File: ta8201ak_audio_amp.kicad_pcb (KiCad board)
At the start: 2 copper layers, 40.3 x 38 mm, 16 parts, among them J1 INPUT, J2 OUTPUT, J3 POWER, U1 TA8201AK

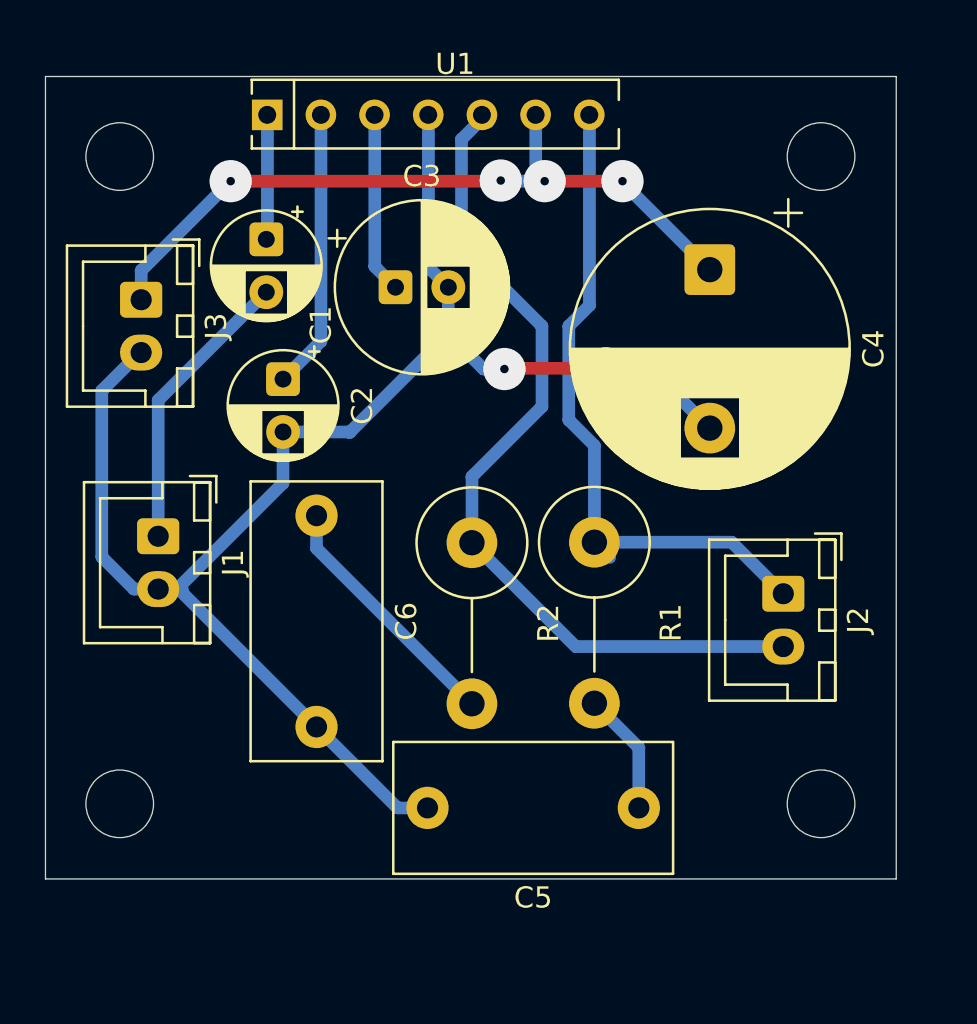
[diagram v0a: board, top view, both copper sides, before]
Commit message: 抵抗560Ωを追加Cを3.3uF,33uFに変更
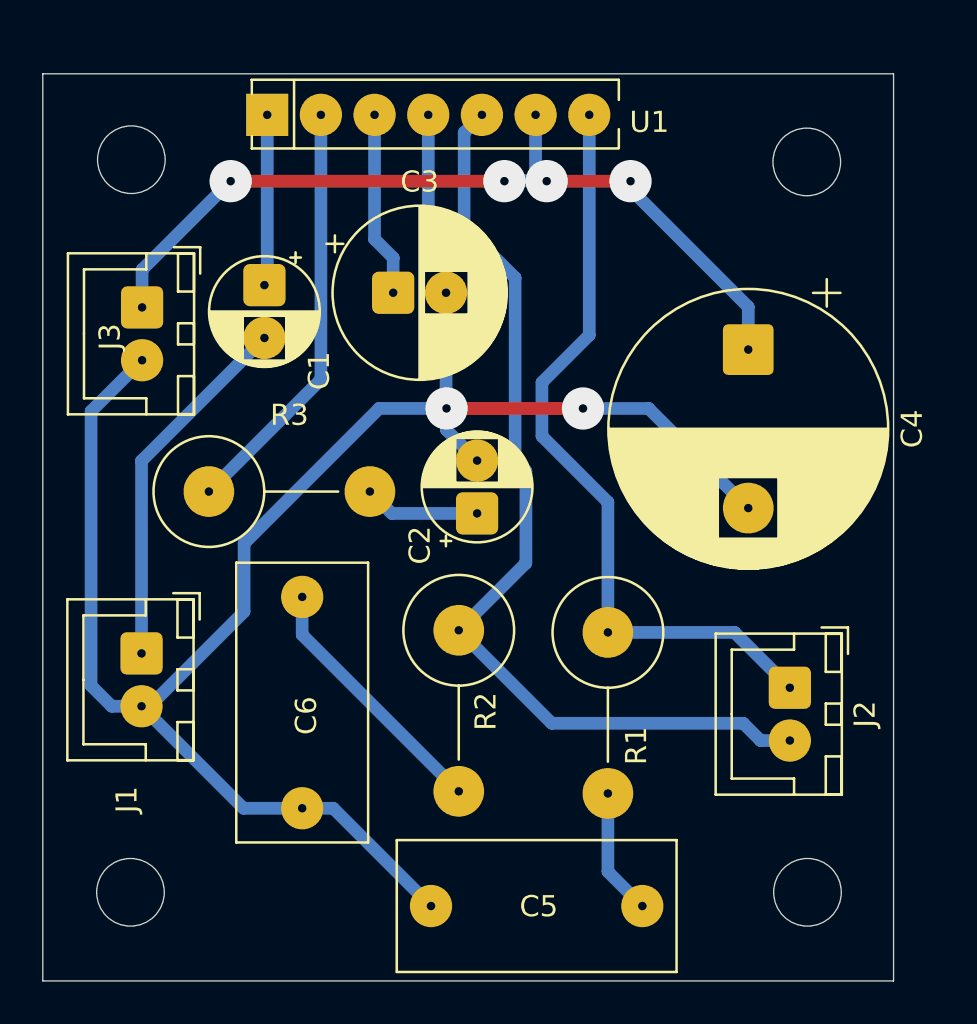
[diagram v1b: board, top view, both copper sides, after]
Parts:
- added R3: 560, Resistor_THT:R_Axial_DIN0516_L15.5mm_D5.0mm_P7.62mm_Vertical, F.Cu at (118.6, 66.8)
- C1: value 4.7uF -> 3.3uF
- C2: value 47uF -> 33uF
- moved C2 11.2 mm to (131.3, 67.8), turned to 90 degrees
- moved J1 5.60 mm to (115.4, 74.4)
- moved C5 4.65 mm to (139.1, 86.4)
- moved J2 4.46 mm to (146.1, 76.0)
- moved R1 4.32 mm to (137.5, 73.4)
- moved H4 4.24 mm to (146.9, 85.7)
- moved H3 4.22 mm to (114.9, 85.7)
- moved C4 4.20 mm to (144.1, 60.0)
- moved R2 4.19 mm to (130.4, 73.3)
- moved C6 3.91 mm to (123.0, 71.7)
- moved C1 2.17 mm to (121.2, 57.0)
- moved H2 0.72 mm to (146.9, 51.2)
- moved H1 0.57 mm to (114.9, 51.1)
- moved J3 0.37 mm to (115.4, 58.0)
- moved C3 0.28 mm to (127.3, 57.4)
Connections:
- C2 pad 1: Net-(U1-NF) -> Net-(C2-Pad1)
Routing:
- net GND: track 78.3 -> 93.3 mm
- net Net-(U1-NF): track 13.1 -> 20.0 mm
- net VCC: track 36.1 -> 41.7 mm
- net Net-(C2-Pad1): track 0.00 -> 5.50 mm
- net Net-(J2-Pin_2): track 40.5 -> 45.5 mm
- net Net-(J2-Pin_1): track 31.9 -> 36.4 mm
- net Net-(C1-Pad2): track 13.7 -> 17.3 mm
- net Net-(U1-IN): track 5.73 -> 8.11 mm
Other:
- board size 40.3 x 38 mm -> 40.3 x 42.9 mm

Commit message: 配置の修正
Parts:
- moved C4 1.64 mm to (144.1, 61.7), turned to 180 degrees
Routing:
- net GND: track 93.3 -> 84.3 mm, vias 2 -> 1
- net Net-(J2-Pin_2): track 45.5 -> 51.7 mm
- net VCC: track 41.7 -> 43.2 mm
- net Net-(J2-Pin_1): track 36.4 -> 37.8 mm

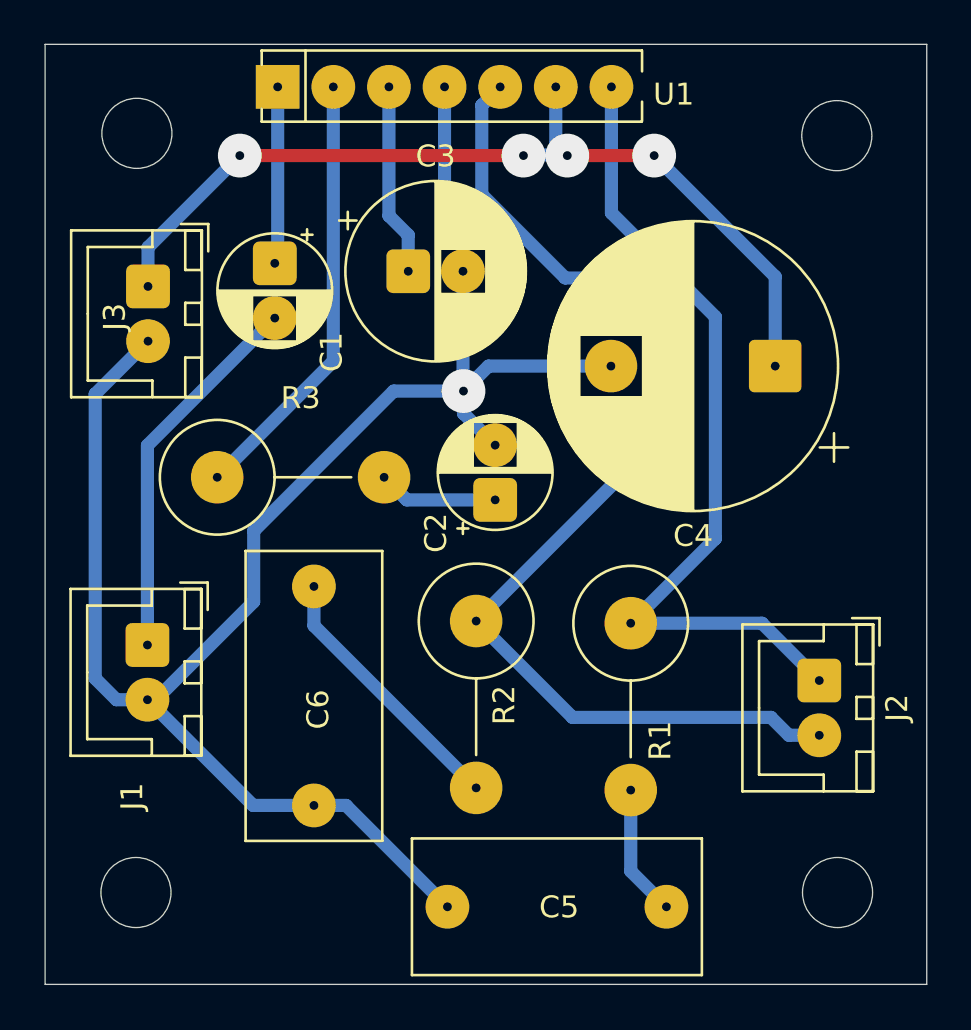
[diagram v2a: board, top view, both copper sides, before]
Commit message: 配置変更、ジャンパを減らす。
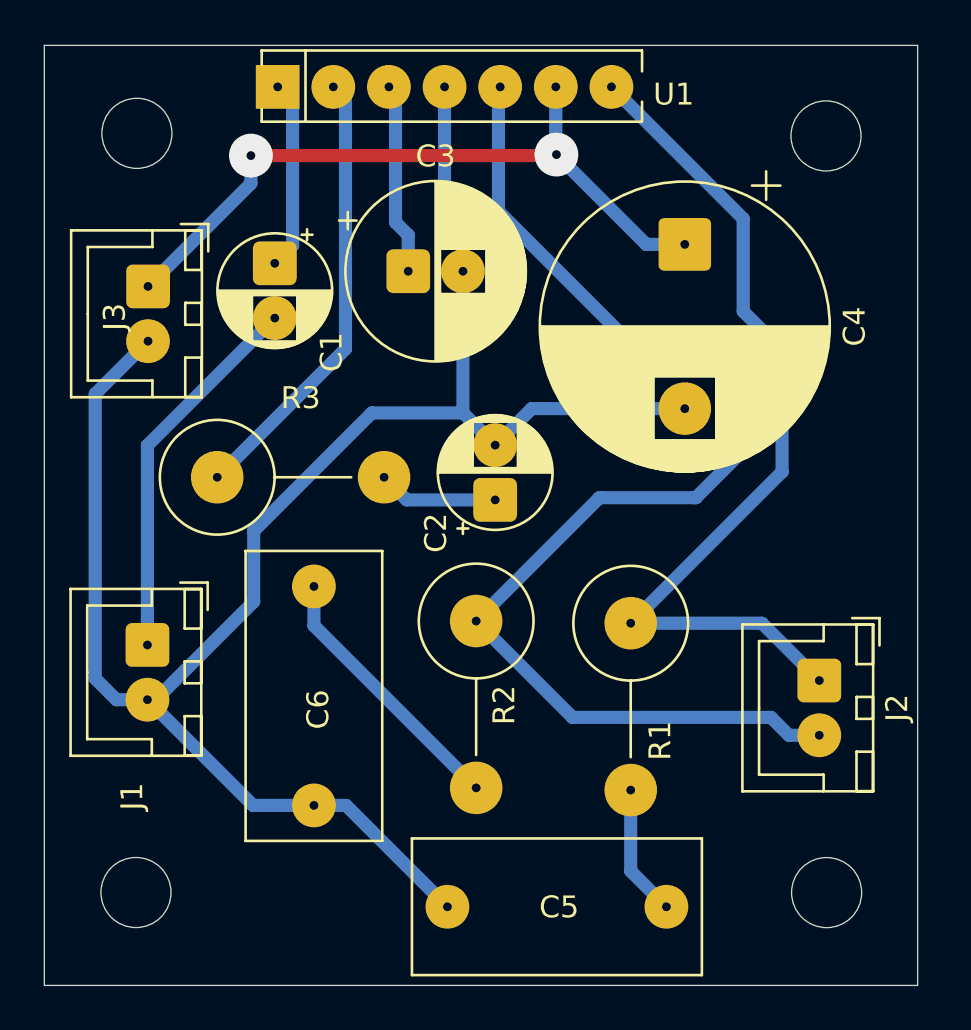
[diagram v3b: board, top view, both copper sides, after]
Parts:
- moved C4 6.92 mm to (140.0, 56.1), turned to -90 degrees
- moved H4 0.50 mm to (146.4, 85.7)
- moved H2 0.49 mm to (146.4, 51.2)
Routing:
- net VCC: track 43.2 -> 34.5 mm, vias 4 -> 2
- net Net-(J2-Pin_2): track 51.7 -> 57.3 mm
- net Net-(J2-Pin_1): track 37.8 -> 40.3 mm
- net GND: track 84.3 -> 85.7 mm, vias 1 -> 0
- net Net-(U1-IN): track 8.11 -> 8.68 mm
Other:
- board size 40.3 x 42.9 mm -> 39.9 x 42.9 mm

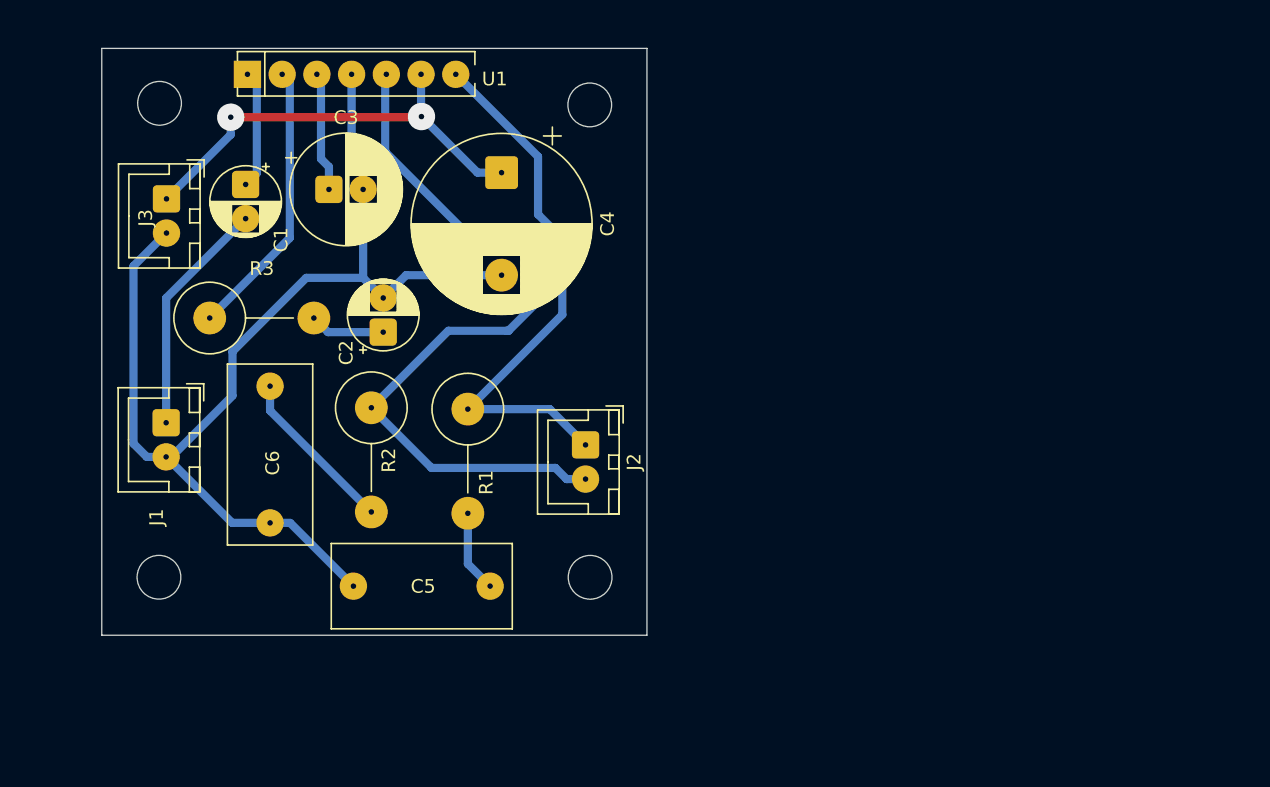
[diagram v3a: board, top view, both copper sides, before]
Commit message: 配置変更、アッテネーター追加、ベタ追加。
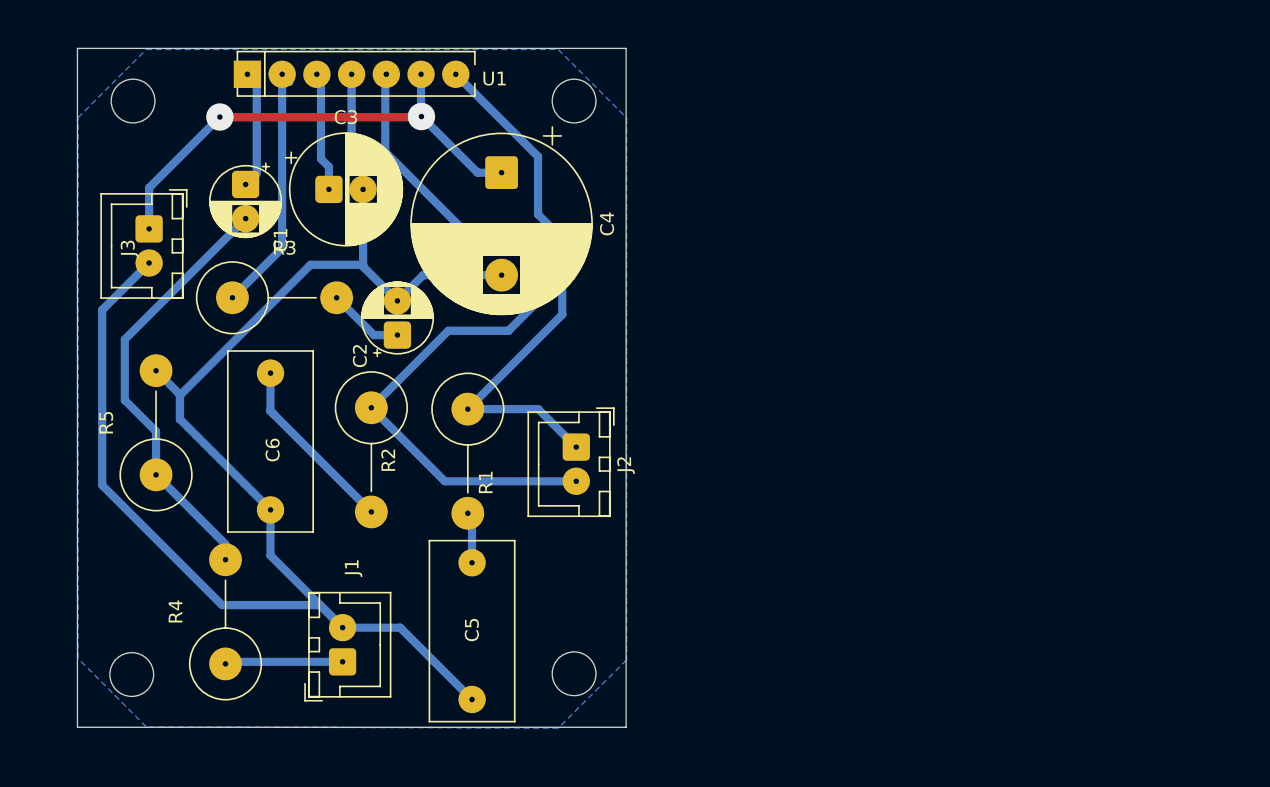
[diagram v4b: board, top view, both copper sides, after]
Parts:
- added R4: 39kΩ, Resistor_THT:R_Axial_DIN0516_L15.5mm_D5.0mm_P7.62mm_Vertical, F.Cu at (119.8, 92.1)
- added R5: 10kΩ, Resistor_THT:R_Axial_DIN0516_L15.5mm_D5.0mm_P7.62mm_Vertical, F.Cu at (114.7, 78.2)
- moved J1 21.7 mm to (128.3, 91.9), turned to 90 degrees
- moved H3 7.39 mm to (112.9, 92.8)
- moved H4 7.15 mm to (145.3, 92.8)
- moved J3 2.54 mm to (114.2, 60.2)
- moved R3 2.23 mm to (120.3, 65.3)
- moved C5 2.16 mm to (137.8, 84.7), turned to -90 degrees
- moved H1 1.94 mm to (113.0, 50.9)
- moved H2 1.18 mm to (145.3, 50.9)
- moved C2 1.06 mm to (132.3, 68.0)
- moved C6 0.95 mm to (123.1, 70.8)
- moved J2 0.70 mm to (145.4, 76.2)
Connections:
- J1 pad T: Net-(C1-Pad2) -> Net-(J1-PadT)
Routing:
- net GND: track 85.7 -> 122.1 mm
- net Net-(C1-Pad2): track 17.3 -> 31.7 mm
- net Net-(J1-PadT): track 0.00 -> 8.63 mm
- net VCC: track 34.5 -> 36.9 mm
- net Net-(C5-Pad1): track 6.00 -> 3.75 mm
- net Net-(U1-NF): track 20.5 -> 18.6 mm
- net Net-(C6-Pad1): track 12.3 -> 13.6 mm
- net Net-(J2-Pin_2): track 57.3 -> 56.7 mm
- net Net-(J2-Pin_1): track 40.3 -> 39.7 mm
- added copper zone on B.Cu, net (none)
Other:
- board size 39.9 x 42.9 mm -> 40.1 x 49.7 mm

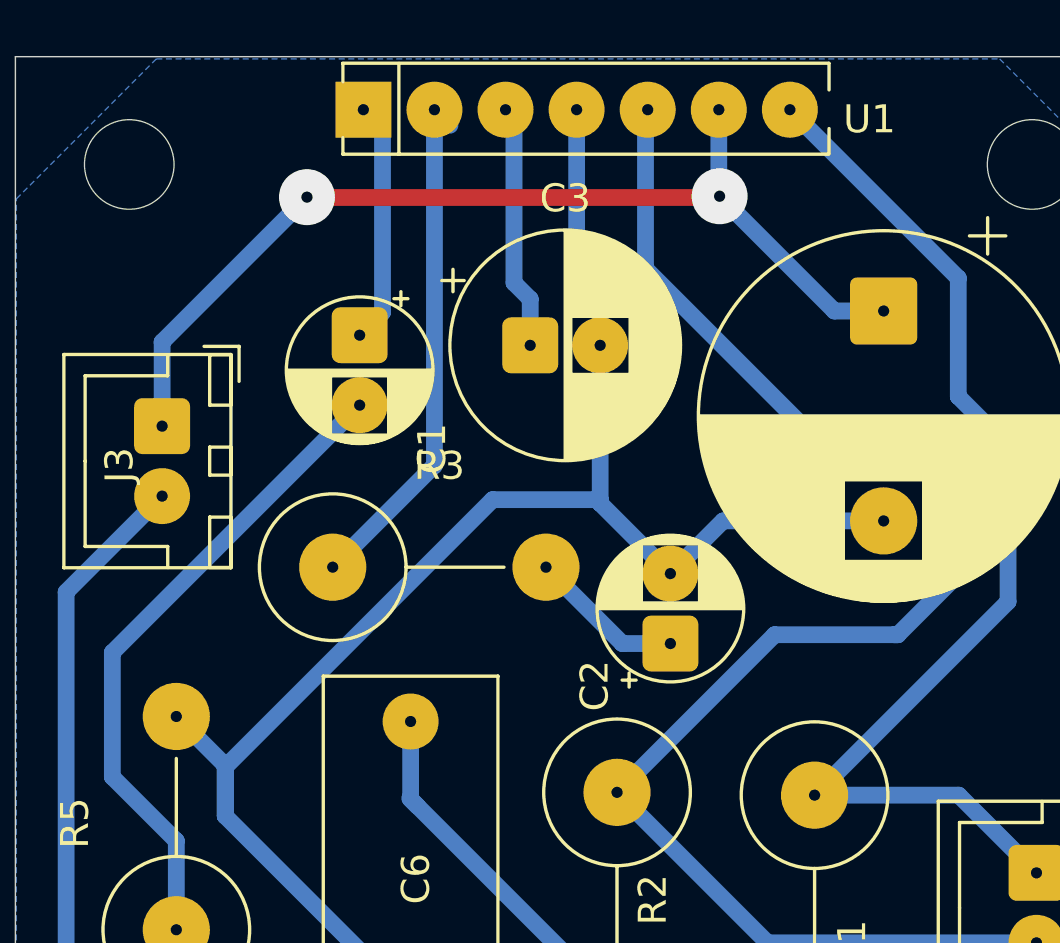
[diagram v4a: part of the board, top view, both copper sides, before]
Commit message: 電解コンデンサの足幅修正
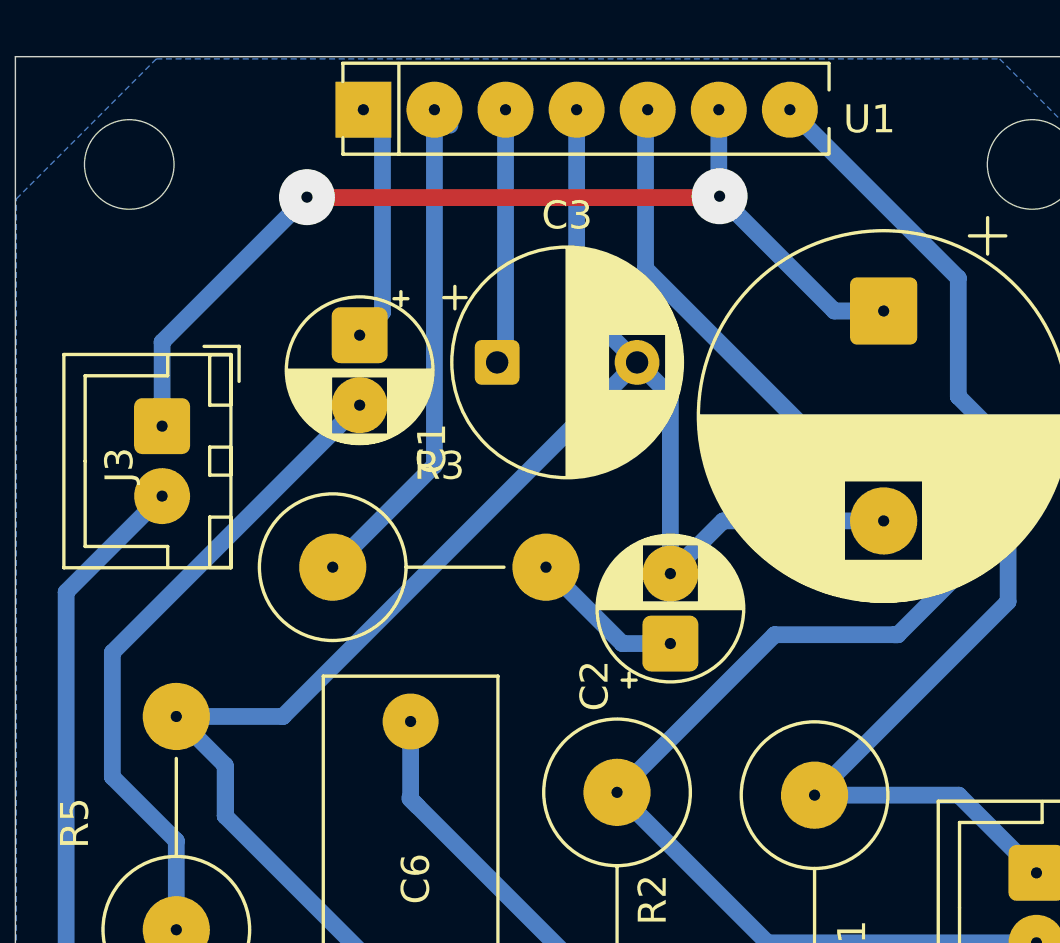
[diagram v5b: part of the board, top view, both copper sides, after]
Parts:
- C1: value 3.3uF -> 4.7uF
- C2: value 33uF -> 47uF
- C3: footprint Capacitor_THT:CP_Radial_D8.0mm_P2.50mm -> Capacitor_THT:CP_Radial_D8.0mm_P5.00mm
- R3: value 560 -> 1.5k
- moved C3 1.33 mm to (126.1, 58.0)
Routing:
- net GND: track 122.1 -> 126.0 mm
- net Net-(U1-R.F): track 8.78 -> 9.58 mm
